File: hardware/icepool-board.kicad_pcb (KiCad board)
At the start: 4 copper layers, 66 x 65 mm, 181 parts, among them J1 8P8C_Shielded, J2 8P8C_Shielded, J3 I2C, J4 USB_B_Micro, J5 SWD, J6 PWR_IN, SW1 B3U-1000P, U1 ISL83488/ISL83490, U2 ATSAMD21E, U3 iCE40HX8K-BG121(121-Ball_caBG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, U4 iCE40HX8K-BG121(121-Ball_caBG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, U5 iCE40HX8K-BG121(121-Ball_caBG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, U6 iCE40HX8K-BG121(121-Ball_caBG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, U7 FAN2306, U8 TPS7150, U9 FAN2306, X1 CB3LV-3I-16M0000, X2 CB3LV-3I-16M0000, X3 CB3LV-3I-16M0000, X4 CB3LV-3I-16M0000, Y1 16MHz

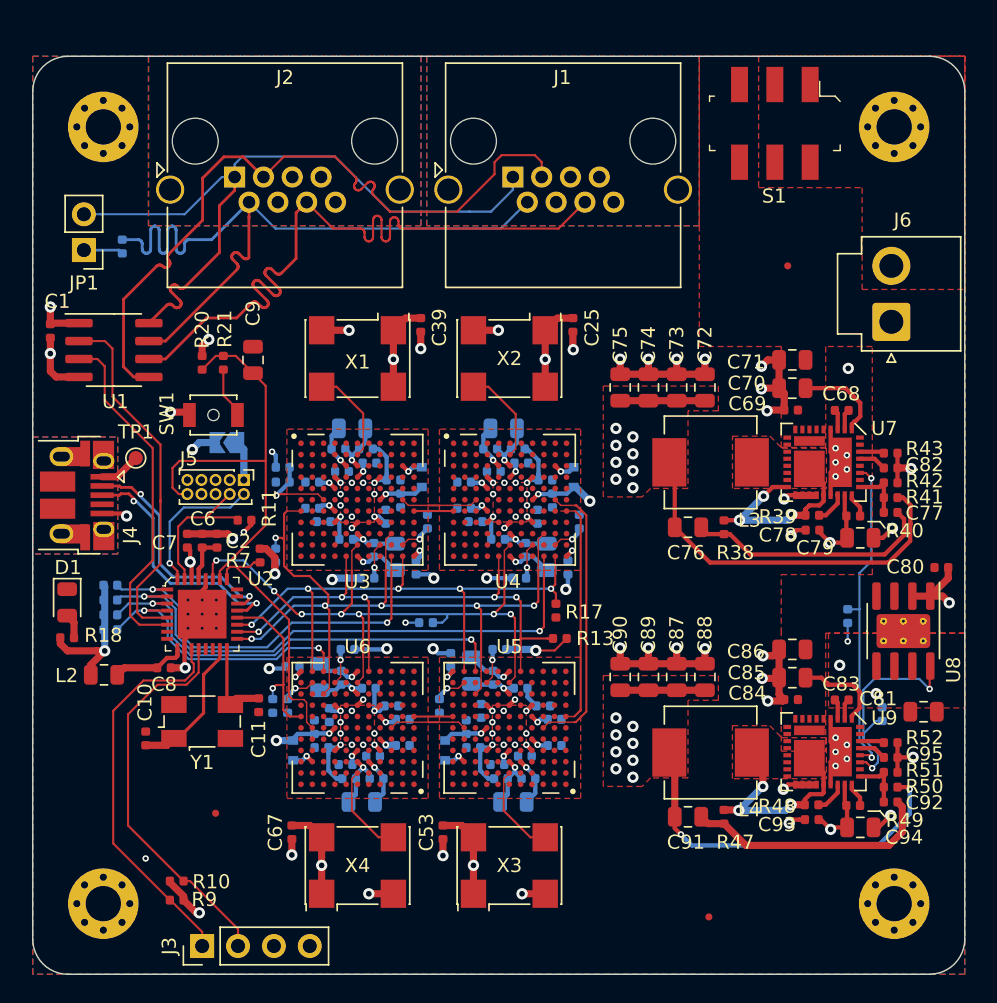
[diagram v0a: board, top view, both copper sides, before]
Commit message: Double checking buck layout, step 1.
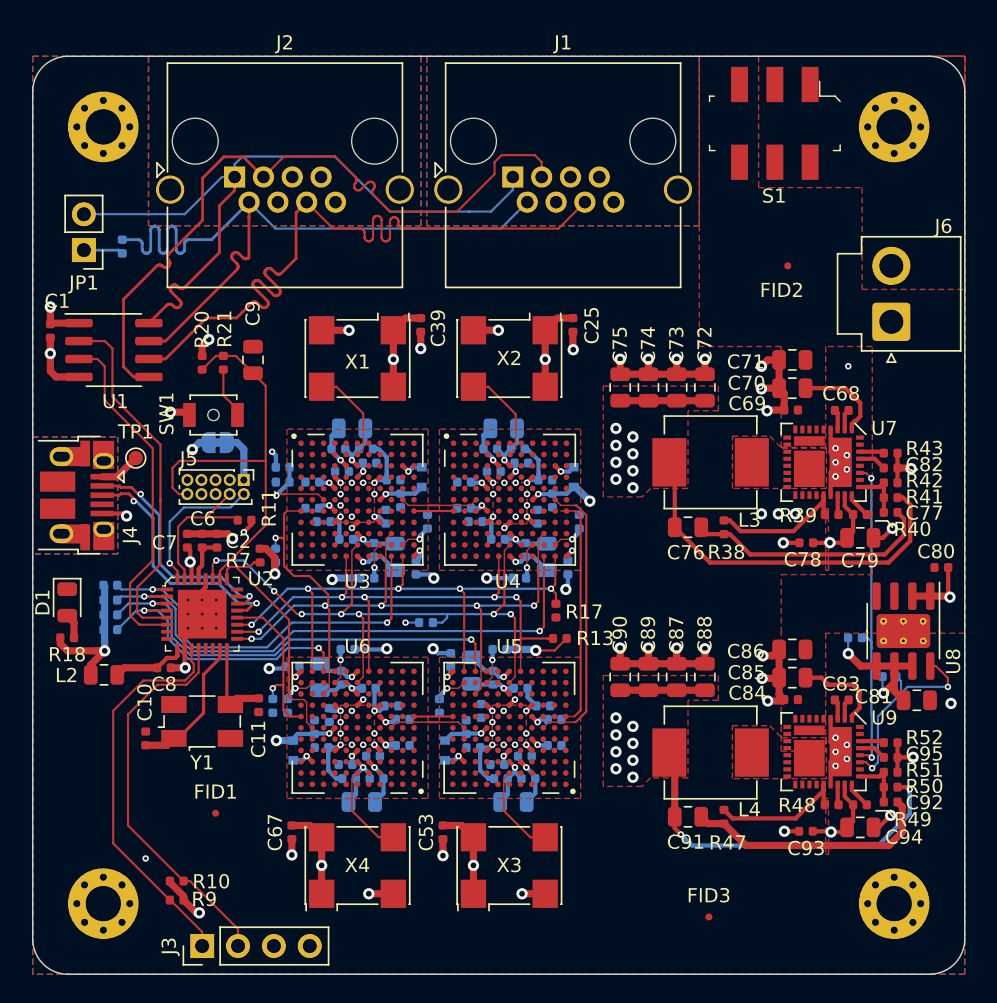
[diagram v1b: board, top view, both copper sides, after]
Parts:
- removed R12: 0R, Jumper:SolderJumper-2_P1.3mm_Open_TrianglePad1.0x1.5mm
- added JP2: SWD_VBUS, Jumper:SolderJumper-2_P1.3mm_Bridged_RoundedPad1.0x1.5mm, B.Cu at (123.1, 102.3)
- moved R44 2.70 mm to (170.7, 118.9), turned to 0 degrees
- moved R45 1.62 mm to (168.2, 116.2), turned to 0 degrees
- moved R48 1.42 mm to (166.6, 128.0)
- moved R39 1.38 mm to (166.6, 107.5)
- moved C78 1.00 mm to (164.8, 109.5)
- moved C81 0.94 mm to (172.6, 120.6)
- moved C93 0.92 mm to (164.8, 129.9)
- moved R40 0.49 mm to (168.6, 107.5)
- moved R49 0.48 mm to (168.6, 128.0)
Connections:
- net Net-(C68-Pad1) renamed /Power/SW_3v3
- net Net-(C83-Pad1) renamed /Power/SW_1v2
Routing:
- net +5V: track 45.9 -> 54.8 mm, vias 5 -> 4
- net /Power/SW_1v2: track 17.2 -> 11.5 mm, vias 3 -> 0
- net /Power/SW_3v3: track 16.5 -> 11.6 mm, vias 3 -> 0
- net GND: track 103.8 -> 101.2 mm, vias 77 -> 79
- net PG_0: track 16.2 -> 14.6 mm
- net Net-(R39-Pad2): track 2.31 -> 1.40 mm
- net Net-(R48-Pad2): track 2.30 -> 1.46 mm
- net Net-(J5-Pad1): track 2.85 -> 3.57 mm
- net +3V3: track 215.4 -> 214.9 mm
- added copper zone on B.Cu, net Net-(J1-PadSH)
- added copper zone on B.Cu, net Net-(J2-PadSH)
- removed copper zone on B.Cu, net (none)
- removed copper zone on F.Cu, net +5V

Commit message: Isolated F copper ground fill on power supplies.
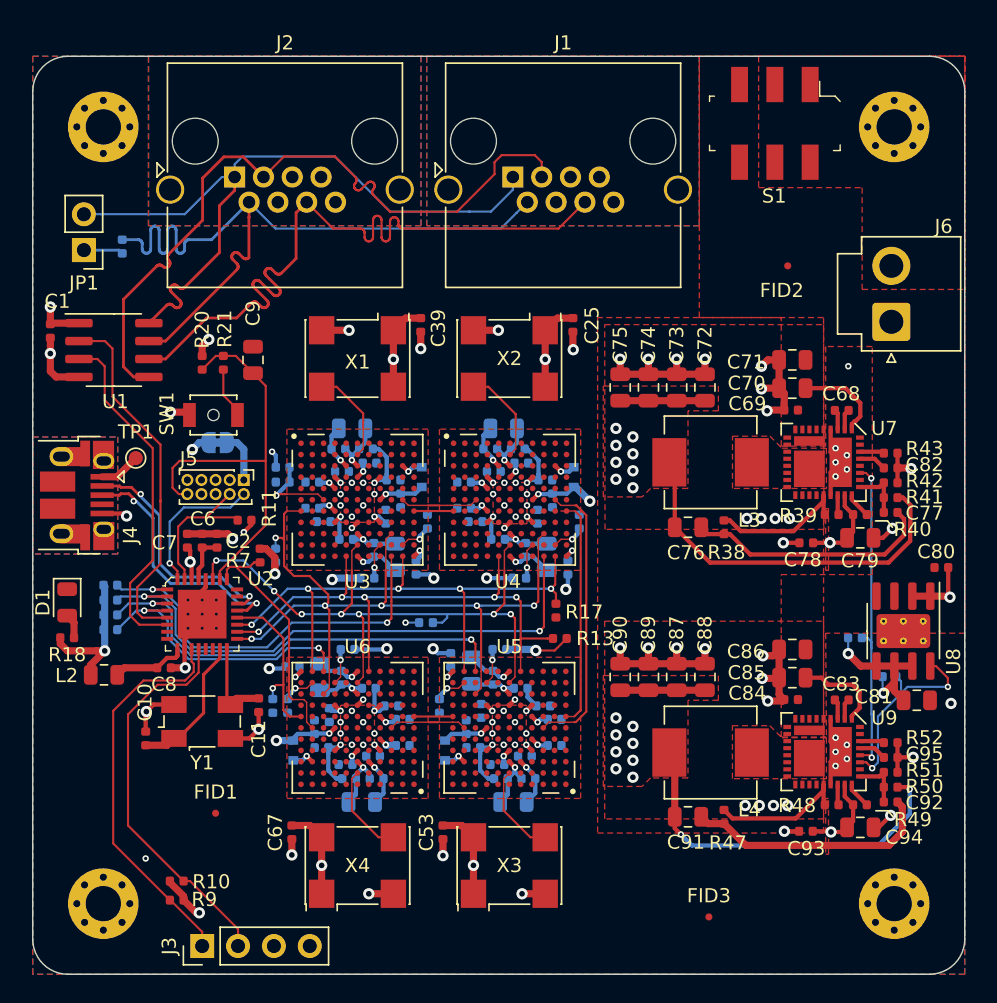
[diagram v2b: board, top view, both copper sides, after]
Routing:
- net GND: track 101.2 -> 108.3 mm, vias 79 -> 90
- net +3V3: track 214.9 -> 218.1 mm
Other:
- net class Default: clearance 0.127 -> 0.0889
- rule trace_clearance: 0.127 -> 0.0889

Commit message: Finalizing board.
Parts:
- added TP2: 3V3 Test, TestPoint:TestPoint_Pad_D1.0mm, F.Cu at (152.1, 108.0)
- added TP3: 5V Test, TestPoint:TestPoint_Pad_D1.0mm, F.Cu at (161.5, 112.8)
- added TP4: 1V2 Test, TestPoint:TestPoint_Pad_D1.0mm, F.Cu at (151.8, 128.7)
- moved FID3 6.89 mm to (151.8, 132.7)
- moved FID1 3.33 mm to (125.9, 127.0)
- moved R10 1.49 mm to (119.2, 132.3)
- moved R9 1.49 mm to (119.2, 133.7)
- moved C69 0.50 mm to (163.2, 100.0)
- moved C70 0.50 mm to (163.3, 98.5)
- moved C71 0.50 mm to (163.3, 96.5)
- moved C76 0.50 mm to (156.4, 108.8)
- moved C84 0.50 mm to (163.2, 120.5)
- moved C85 0.50 mm to (163.3, 119.0)
- moved C86 0.50 mm to (163.3, 117.0)
- moved C91 0.50 mm to (156.4, 129.3)
- moved R38 0.50 mm to (158.9, 108.8)
- moved R47 0.50 mm to (158.9, 129.3)
- moved J1 0.20 mm to (144.0, 83.3)
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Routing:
- net GND: track 108.3 -> 72.5 mm, vias 90 -> 67
- net +1V2: track 73.9 -> 79.8 mm
- net VCC: track 12.8 -> 6.96 mm
- net +5V: track 54.8 -> 60.3 mm, vias 4 -> 5
- net +3V3: track 218.1 -> 221.9 mm
- net /RX+: track 50.8 -> 53.5 mm
- net Net-(C91-Pad2): track 17.7 -> 19.2 mm, vias 0 -> 2
- net /Power/SW_1v2: track 11.5 -> 10.0 mm, vias 0 -> 2
- net /Power/SW_3v3: track 11.6 -> 10.5 mm, vias 0 -> 2
- net /TX+: track 51.0 -> 52.0 mm
- net /TX-: track 51.0 -> 52.0 mm
- net /RX-: track 54.7 -> 55.5 mm
- removed copper zone on B.Cu, net Net-(J1-PadSH)
- removed copper zone on F.Cu, net Net-(J1-PadSH)
- removed copper zone on In1.Cu, net Net-(J1-PadSH)
- removed copper zone on In2.Cu, net Net-(J1-PadSH)
- removed copper zone on B.Cu, net Net-(J2-PadSH)
- removed copper zone on F.Cu, net Net-(J2-PadSH)
- removed copper zone on In1.Cu, net Net-(J2-PadSH)
- removed copper zone on In2.Cu, net Net-(J2-PadSH)
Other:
- board text added: "+12V"
- board text added: "3V3"
- board text added: "GND"
- board text added: "SCL"
- board text added: "SDA"
- board text added: "icepool fourside.io"

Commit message: Generated gerbers. Ordered.
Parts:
- added FID4: Fiducial, Fiducial:Fiducial_0.5mm_Mask1mm, B.Cu at (166.8, 119.6)
- added FID5: Fiducial, Fiducial:Fiducial_0.5mm_Mask1mm, B.Cu at (138.6, 99.0)
- added FID6: Fiducial, Fiducial:Fiducial_0.5mm_Mask1mm, B.Cu at (135.3, 130.8)
- TP1, TP2, TP3, TP4: footprint TestPoint:TestPoint_Pad_D1.0mm -> TestPoint:TestPoint_Keystone_5000-5004_Miniature
- moved TP1 4.97 mm to (113.5, 100.2)
- moved TP2 2.40 mm to (152.2, 110.4)
- moved FID3 1.73 mm to (150.8, 134.2)
- moved TP4 1.56 mm to (151.6, 130.2)
- moved C69 0.30 mm to (163.2, 99.8)
- moved C70 0.30 mm to (163.3, 98.2)
- moved C71 0.30 mm to (163.3, 96.2)
- moved C84 0.30 mm to (163.2, 120.2)
- moved C85 0.30 mm to (163.3, 118.7)
- moved C86 0.30 mm to (163.3, 116.7)
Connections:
- J1 pad 4: (no net) -> Net-(J1-Pad4)
- J1 pad 5: (no net) -> Net-(J1-Pad5)
- J1 pad 7: (no net) -> Net-(J1-Pad7)
- J1 pad 8: (no net) -> Net-(J1-Pad8)
- J2 pad 4: (no net) -> Net-(J2-Pad4)
- J2 pad 5: (no net) -> Net-(J2-Pad5)
- J2 pad 7: (no net) -> Net-(J2-Pad7)
- J2 pad 8: (no net) -> Net-(J2-Pad8)
- J4 pad 4: (no net) -> Net-(J4-Pad4)
- J5 pad 6: (no net) -> Net-(J5-Pad6)
- J5 pad 8: (no net) -> Net-(J5-Pad8)
- S1 pad 1: (no net) -> Net-(S1-Pad1)
- S1 pad 4: (no net) -> Net-(S1-Pad4)
- U2 pad 13: (no net) -> Net-(U2-Pad13)
- U2 pad 14: (no net) -> Net-(U2-Pad14)
- U2 pad 23: (no net) -> Net-(U2-Pad23)
- U2 pad 24: (no net) -> Net-(U2-Pad24)
- U2 pad 7: (no net) -> Net-(U2-Pad7)
- U2 pad 8: (no net) -> Net-(U2-Pad8)
- U3 pad A1: (no net) -> Net-(U3-PadA1)
- U3 pad A10: (no net) -> Net-(U3-PadA10)
- U3 pad A11: (no net) -> Net-(U3-PadA11)
- U3 pad A2: (no net) -> Net-(U3-PadA2)
- U3 pad A3: (no net) -> Net-(U3-PadA3)
- U3 pad A4: (no net) -> Net-(U3-PadA4)
- U3 pad A5: (no net) -> Net-(U3-PadA5)
- U3 pad A6: (no net) -> Net-(U3-PadA6)
- U3 pad A7: (no net) -> Net-(U3-PadA7)
- U3 pad A8: (no net) -> Net-(U3-PadA8)
- U3 pad A9: (no net) -> Net-(U3-PadA9)
- U3 pad B1: (no net) -> Net-(U3-PadB1)
- U3 pad B10: (no net) -> Net-(U3-PadB10)
- U3 pad B11: (no net) -> Net-(U3-PadB11)
- U3 pad B2: (no net) -> Net-(U3-PadB2)
- U3 pad B3: (no net) -> Net-(U3-PadB3)
- U3 pad B4: (no net) -> Net-(U3-PadB4)
- U3 pad B5: (no net) -> Net-(U3-PadB5)
- U3 pad B7: (no net) -> Net-(U3-PadB7)
- U3 pad B8: (no net) -> Net-(U3-PadB8)
- U3 pad B9: (no net) -> Net-(U3-PadB9)
- U3 pad C1: (no net) -> Net-(U3-PadC1)
- U3 pad C11: (no net) -> Net-(U3-PadC11)
- U3 pad C2: (no net) -> Net-(U3-PadC2)
- U3 pad C3: (no net) -> Net-(U3-PadC3)
- U3 pad C4: (no net) -> Net-(U3-PadC4)
- U3 pad C7: (no net) -> Net-(U3-PadC7)
- U3 pad C8: (no net) -> Net-(U3-PadC8)
- U3 pad C9: (no net) -> Net-(U3-PadC9)
- U3 pad D1: (no net) -> Net-(U3-PadD1)
- U3 pad D10: (no net) -> Net-(U3-PadD10)
- U3 pad D11: (no net) -> Net-(U3-PadD11)
- U3 pad D2: (no net) -> Net-(U3-PadD2)
- U3 pad D3: (no net) -> Net-(U3-PadD3)
- U3 pad D5: (no net) -> Net-(U3-PadD5)
- U3 pad D7: (no net) -> Net-(U3-PadD7)
- U3 pad D9: (no net) -> Net-(U3-PadD9)
- U3 pad E1: (no net) -> Net-(U3-PadE1)
- U3 pad E10: (no net) -> Net-(U3-PadE10)
- U3 pad E11: (no net) -> Net-(U3-PadE11)
- U3 pad E2: (no net) -> Net-(U3-PadE2)
- U3 pad E3: (no net) -> Net-(U3-PadE3)
- U3 pad E8: (no net) -> Net-(U3-PadE8)
- U3 pad E9: (no net) -> Net-(U3-PadE9)
- U3 pad F1: (no net) -> Net-(U3-PadF1)
- U3 pad F11: (no net) -> Net-(U3-PadF11)
- U3 pad F2: (no net) -> Net-(U3-PadF2)
- U3 pad F4: (no net) -> Net-(U3-PadF4)
- U3 pad F9: (no net) -> Net-(U3-PadF9)
- U3 pad G10: (no net) -> Net-(U3-PadG10)
- U3 pad G2: (no net) -> Net-(U3-PadG2)
- U3 pad G3: (no net) -> Net-(U3-PadG3)
- U3 pad G8: (no net) -> Net-(U3-PadG8)
- U3 pad G9: (no net) -> Net-(U3-PadG9)
- U3 pad H1: (no net) -> Net-(U3-PadH1)
- U3 pad H10: (no net) -> Net-(U3-PadH10)
- U3 pad H11: (no net) -> Net-(U3-PadH11)
- U3 pad H2: (no net) -> Net-(U3-PadH2)
- U3 pad H3: (no net) -> Net-(U3-PadH3)
- U3 pad H7: (no net) -> Net-(U3-PadH7)
- U3 pad H9: (no net) -> Net-(U3-PadH9)
- U3 pad J1: (no net) -> Net-(U3-PadJ1)
- U3 pad J10: (no net) -> Net-(U3-PadJ10)
- U3 pad J11: (no net) -> Net-(U3-PadJ11)
- U3 pad J2: (no net) -> Net-(U3-PadJ2)
- U3 pad J3: (no net) -> Net-(U3-PadJ3)
- U3 pad J4: (no net) -> Net-(U3-PadJ4)
- U3 pad J5: (no net) -> Net-(U3-PadJ5)
- U3 pad J7: (no net) -> Net-(U3-PadJ7)
- U3 pad J8: (no net) -> Net-(U3-PadJ8)
- U3 pad K1: (no net) -> Net-(U3-PadK1)
- U3 pad K11: (no net) -> Net-(U3-PadK11)
- U3 pad K2: (no net) -> Net-(U3-PadK2)
- U3 pad K3: (no net) -> Net-(U3-PadK3)
- U3 pad K4: (no net) -> Net-(U3-PadK4)
- U3 pad K5: (no net) -> Net-(U3-PadK5)
- U3 pad K7: (no net) -> Net-(U3-PadK7)
- U3 pad K9: (no net) -> /ICE40HX8K-BG121_0/GMISO
- U3 pad L1: (no net) -> Net-(U3-PadL1)
- U3 pad L2: (no net) -> Net-(U3-PadL2)
- U3 pad L3: (no net) -> Net-(U3-PadL3)
- U3 pad L4: (no net) -> Net-(U3-PadL4)
- U3 pad L7: (no net) -> Net-(U3-PadL7)
- U3 pad L8: (no net) -> Net-(U3-PadL8)
- U4 pad A1: (no net) -> Net-(U4-PadA1)
- U4 pad A10: (no net) -> Net-(U4-PadA10)
- U4 pad A11: (no net) -> Net-(U4-PadA11)
- U4 pad A2: (no net) -> Net-(U4-PadA2)
- U4 pad A3: (no net) -> Net-(U4-PadA3)
- U4 pad A4: (no net) -> Net-(U4-PadA4)
- U4 pad A5: (no net) -> Net-(U4-PadA5)
- U4 pad A6: (no net) -> Net-(U4-PadA6)
- U4 pad A7: (no net) -> Net-(U4-PadA7)
- U4 pad A8: (no net) -> Net-(U4-PadA8)
- U4 pad A9: (no net) -> Net-(U4-PadA9)
- U4 pad B1: (no net) -> Net-(U4-PadB1)
- U4 pad B10: (no net) -> Net-(U4-PadB10)
- U4 pad B11: (no net) -> Net-(U4-PadB11)
- U4 pad B2: (no net) -> Net-(U4-PadB2)
- U4 pad B3: (no net) -> Net-(U4-PadB3)
- U4 pad B4: (no net) -> Net-(U4-PadB4)
- U4 pad B5: (no net) -> Net-(U4-PadB5)
- U4 pad B7: (no net) -> Net-(U4-PadB7)
- U4 pad B8: (no net) -> Net-(U4-PadB8)
- U4 pad B9: (no net) -> Net-(U4-PadB9)
- U4 pad C1: (no net) -> Net-(U4-PadC1)
- U4 pad C11: (no net) -> Net-(U4-PadC11)
- U4 pad C2: (no net) -> Net-(U4-PadC2)
- U4 pad C3: (no net) -> Net-(U4-PadC3)
- U4 pad C4: (no net) -> Net-(U4-PadC4)
- U4 pad C7: (no net) -> Net-(U4-PadC7)
- U4 pad C8: (no net) -> Net-(U4-PadC8)
- U4 pad C9: (no net) -> Net-(U4-PadC9)
- U4 pad D1: (no net) -> Net-(U4-PadD1)
- U4 pad D10: (no net) -> Net-(U4-PadD10)
- U4 pad D11: (no net) -> Net-(U4-PadD11)
- U4 pad D2: (no net) -> Net-(U4-PadD2)
- U4 pad D3: (no net) -> Net-(U4-PadD3)
- U4 pad D5: (no net) -> Net-(U4-PadD5)
- U4 pad D7: (no net) -> Net-(U4-PadD7)
- U4 pad D9: (no net) -> Net-(U4-PadD9)
- U4 pad E1: (no net) -> Net-(U4-PadE1)
- U4 pad E10: (no net) -> Net-(U4-PadE10)
- U4 pad E11: (no net) -> Net-(U4-PadE11)
- U4 pad E2: (no net) -> Net-(U4-PadE2)
- U4 pad E3: (no net) -> Net-(U4-PadE3)
- U4 pad E8: (no net) -> Net-(U4-PadE8)
- U4 pad E9: (no net) -> Net-(U4-PadE9)
- U4 pad F1: (no net) -> Net-(U4-PadF1)
- U4 pad F11: (no net) -> Net-(U4-PadF11)
- U4 pad F2: (no net) -> Net-(U4-PadF2)
- U4 pad F4: (no net) -> Net-(U4-PadF4)
- U4 pad F9: (no net) -> Net-(U4-PadF9)
- U4 pad G10: (no net) -> Net-(U4-PadG10)
- U4 pad G2: (no net) -> Net-(U4-PadG2)
- U4 pad G3: (no net) -> Net-(U4-PadG3)
- U4 pad G8: (no net) -> Net-(U4-PadG8)
- U4 pad G9: (no net) -> Net-(U4-PadG9)
- U4 pad H1: (no net) -> Net-(U4-PadH1)
- U4 pad H10: (no net) -> Net-(U4-PadH10)
- U4 pad H11: (no net) -> Net-(U4-PadH11)
- U4 pad H2: (no net) -> Net-(U4-PadH2)
- U4 pad H3: (no net) -> Net-(U4-PadH3)
- U4 pad H7: (no net) -> Net-(U4-PadH7)
- U4 pad H9: (no net) -> Net-(U4-PadH9)
- U4 pad J1: (no net) -> Net-(U4-PadJ1)
- U4 pad J10: (no net) -> Net-(U4-PadJ10)
- U4 pad J11: (no net) -> Net-(U4-PadJ11)
- U4 pad J2: (no net) -> Net-(U4-PadJ2)
- U4 pad J3: (no net) -> Net-(U4-PadJ3)
- U4 pad J4: (no net) -> Net-(U4-PadJ4)
- U4 pad J5: (no net) -> Net-(U4-PadJ5)
- U4 pad J7: (no net) -> Net-(U4-PadJ7)
- U4 pad J8: (no net) -> Net-(U4-PadJ8)
- U4 pad K1: (no net) -> Net-(U4-PadK1)
- U4 pad K11: (no net) -> Net-(U4-PadK11)
- U4 pad K2: (no net) -> Net-(U4-PadK2)
- U4 pad K3: (no net) -> Net-(U4-PadK3)
- U4 pad K4: (no net) -> Net-(U4-PadK4)
- U4 pad K5: (no net) -> Net-(U4-PadK5)
- U4 pad K7: (no net) -> Net-(U4-PadK7)
- U4 pad K9: (no net) -> /ICE40HX8K-BG121_1/GMISO
- U4 pad L1: (no net) -> Net-(U4-PadL1)
- U4 pad L2: (no net) -> Net-(U4-PadL2)
- U4 pad L3: (no net) -> Net-(U4-PadL3)
- U4 pad L4: (no net) -> Net-(U4-PadL4)
- U4 pad L7: (no net) -> Net-(U4-PadL7)
- U4 pad L8: (no net) -> Net-(U4-PadL8)
- U5 pad A1: (no net) -> Net-(U5-PadA1)
- U5 pad A10: (no net) -> Net-(U5-PadA10)
- U5 pad A11: (no net) -> Net-(U5-PadA11)
- U5 pad A2: (no net) -> Net-(U5-PadA2)
- U5 pad A3: (no net) -> Net-(U5-PadA3)
- U5 pad A4: (no net) -> Net-(U5-PadA4)
- U5 pad A5: (no net) -> Net-(U5-PadA5)
- U5 pad A6: (no net) -> Net-(U5-PadA6)
- U5 pad A7: (no net) -> Net-(U5-PadA7)
- U5 pad A8: (no net) -> Net-(U5-PadA8)
- U5 pad A9: (no net) -> Net-(U5-PadA9)
- U5 pad B1: (no net) -> Net-(U5-PadB1)
- U5 pad B10: (no net) -> Net-(U5-PadB10)
- U5 pad B11: (no net) -> Net-(U5-PadB11)
- U5 pad B2: (no net) -> Net-(U5-PadB2)
- U5 pad B3: (no net) -> Net-(U5-PadB3)
- U5 pad B4: (no net) -> Net-(U5-PadB4)
- U5 pad B5: (no net) -> Net-(U5-PadB5)
- U5 pad B7: (no net) -> Net-(U5-PadB7)
- U5 pad B8: (no net) -> Net-(U5-PadB8)
- U5 pad B9: (no net) -> Net-(U5-PadB9)
- U5 pad C1: (no net) -> Net-(U5-PadC1)
- U5 pad C11: (no net) -> Net-(U5-PadC11)
- U5 pad C2: (no net) -> Net-(U5-PadC2)
- U5 pad C3: (no net) -> Net-(U5-PadC3)
- U5 pad C4: (no net) -> Net-(U5-PadC4)
- U5 pad C7: (no net) -> Net-(U5-PadC7)
- U5 pad C8: (no net) -> Net-(U5-PadC8)
- U5 pad C9: (no net) -> Net-(U5-PadC9)
- U5 pad D1: (no net) -> Net-(U5-PadD1)
- U5 pad D10: (no net) -> Net-(U5-PadD10)
- U5 pad D11: (no net) -> Net-(U5-PadD11)
- U5 pad D2: (no net) -> Net-(U5-PadD2)
- U5 pad D3: (no net) -> Net-(U5-PadD3)
- U5 pad D5: (no net) -> Net-(U5-PadD5)
- U5 pad D7: (no net) -> Net-(U5-PadD7)
- U5 pad D9: (no net) -> Net-(U5-PadD9)
- U5 pad E1: (no net) -> Net-(U5-PadE1)
- U5 pad E10: (no net) -> Net-(U5-PadE10)
- U5 pad E11: (no net) -> Net-(U5-PadE11)
- U5 pad E2: (no net) -> Net-(U5-PadE2)
- U5 pad E3: (no net) -> Net-(U5-PadE3)
- U5 pad E8: (no net) -> Net-(U5-PadE8)
- U5 pad E9: (no net) -> Net-(U5-PadE9)
- U5 pad F1: (no net) -> Net-(U5-PadF1)
- U5 pad F11: (no net) -> Net-(U5-PadF11)
- U5 pad F2: (no net) -> Net-(U5-PadF2)
- U5 pad F4: (no net) -> Net-(U5-PadF4)
- U5 pad F9: (no net) -> Net-(U5-PadF9)
- U5 pad G10: (no net) -> Net-(U5-PadG10)
- U5 pad G2: (no net) -> Net-(U5-PadG2)
- U5 pad G3: (no net) -> Net-(U5-PadG3)
- U5 pad G8: (no net) -> Net-(U5-PadG8)
- U5 pad G9: (no net) -> Net-(U5-PadG9)
- U5 pad H1: (no net) -> Net-(U5-PadH1)
- U5 pad H10: (no net) -> Net-(U5-PadH10)
- U5 pad H11: (no net) -> Net-(U5-PadH11)
- U5 pad H2: (no net) -> Net-(U5-PadH2)
- U5 pad H3: (no net) -> Net-(U5-PadH3)
- U5 pad H7: (no net) -> Net-(U5-PadH7)
- U5 pad H9: (no net) -> Net-(U5-PadH9)
- U5 pad J1: (no net) -> Net-(U5-PadJ1)
- U5 pad J10: (no net) -> Net-(U5-PadJ10)
- U5 pad J11: (no net) -> Net-(U5-PadJ11)
- U5 pad J2: (no net) -> Net-(U5-PadJ2)
- U5 pad J3: (no net) -> Net-(U5-PadJ3)
- U5 pad J4: (no net) -> Net-(U5-PadJ4)
- U5 pad J5: (no net) -> Net-(U5-PadJ5)
- U5 pad J7: (no net) -> Net-(U5-PadJ7)
- U5 pad J8: (no net) -> Net-(U5-PadJ8)
- U5 pad K1: (no net) -> Net-(U5-PadK1)
- U5 pad K11: (no net) -> Net-(U5-PadK11)
- U5 pad K2: (no net) -> Net-(U5-PadK2)
- U5 pad K3: (no net) -> Net-(U5-PadK3)
- U5 pad K4: (no net) -> Net-(U5-PadK4)
- U5 pad K5: (no net) -> Net-(U5-PadK5)
- U5 pad K7: (no net) -> Net-(U5-PadK7)
- U5 pad K9: (no net) -> /ICE40HX8K-BG121_2/GMISO
- U5 pad L1: (no net) -> Net-(U5-PadL1)
- U5 pad L2: (no net) -> Net-(U5-PadL2)
- U5 pad L3: (no net) -> Net-(U5-PadL3)
- U5 pad L4: (no net) -> Net-(U5-PadL4)
- U5 pad L7: (no net) -> Net-(U5-PadL7)
- U5 pad L8: (no net) -> Net-(U5-PadL8)
- U6 pad A1: (no net) -> Net-(U6-PadA1)
- U6 pad A10: (no net) -> Net-(U6-PadA10)
- U6 pad A11: (no net) -> Net-(U6-PadA11)
- U6 pad A2: (no net) -> Net-(U6-PadA2)
- U6 pad A3: (no net) -> Net-(U6-PadA3)
- U6 pad A4: (no net) -> Net-(U6-PadA4)
- U6 pad A5: (no net) -> Net-(U6-PadA5)
- U6 pad A6: (no net) -> Net-(U6-PadA6)
- U6 pad A7: (no net) -> Net-(U6-PadA7)
- U6 pad A8: (no net) -> Net-(U6-PadA8)
- U6 pad A9: (no net) -> Net-(U6-PadA9)
- U6 pad B1: (no net) -> Net-(U6-PadB1)
- U6 pad B10: (no net) -> Net-(U6-PadB10)
- U6 pad B11: (no net) -> Net-(U6-PadB11)
- U6 pad B2: (no net) -> Net-(U6-PadB2)
- U6 pad B3: (no net) -> Net-(U6-PadB3)
- U6 pad B4: (no net) -> Net-(U6-PadB4)
- U6 pad B5: (no net) -> Net-(U6-PadB5)
- U6 pad B7: (no net) -> Net-(U6-PadB7)
- U6 pad B8: (no net) -> Net-(U6-PadB8)
- U6 pad B9: (no net) -> Net-(U6-PadB9)
- U6 pad C1: (no net) -> Net-(U6-PadC1)
- U6 pad C11: (no net) -> Net-(U6-PadC11)
- U6 pad C2: (no net) -> Net-(U6-PadC2)
- U6 pad C3: (no net) -> Net-(U6-PadC3)
- U6 pad C4: (no net) -> Net-(U6-PadC4)
- U6 pad C7: (no net) -> Net-(U6-PadC7)
- U6 pad C8: (no net) -> Net-(U6-PadC8)
- U6 pad C9: (no net) -> Net-(U6-PadC9)
- U6 pad D1: (no net) -> Net-(U6-PadD1)
- U6 pad D10: (no net) -> Net-(U6-PadD10)
- U6 pad D11: (no net) -> Net-(U6-PadD11)
- U6 pad D2: (no net) -> Net-(U6-PadD2)
- U6 pad D3: (no net) -> Net-(U6-PadD3)
- U6 pad D5: (no net) -> Net-(U6-PadD5)
- U6 pad D7: (no net) -> Net-(U6-PadD7)
- U6 pad D9: (no net) -> Net-(U6-PadD9)
- U6 pad E1: (no net) -> Net-(U6-PadE1)
- U6 pad E10: (no net) -> Net-(U6-PadE10)
- U6 pad E11: (no net) -> Net-(U6-PadE11)
- U6 pad E2: (no net) -> Net-(U6-PadE2)
- U6 pad E3: (no net) -> Net-(U6-PadE3)
- U6 pad E8: (no net) -> Net-(U6-PadE8)
- U6 pad E9: (no net) -> Net-(U6-PadE9)
- U6 pad F1: (no net) -> Net-(U6-PadF1)
- U6 pad F11: (no net) -> Net-(U6-PadF11)
- U6 pad F2: (no net) -> Net-(U6-PadF2)
- U6 pad F4: (no net) -> Net-(U6-PadF4)
- U6 pad F9: (no net) -> Net-(U6-PadF9)
- U6 pad G10: (no net) -> Net-(U6-PadG10)
- U6 pad G2: (no net) -> Net-(U6-PadG2)
- U6 pad G3: (no net) -> Net-(U6-PadG3)
- U6 pad G8: (no net) -> Net-(U6-PadG8)
- U6 pad G9: (no net) -> Net-(U6-PadG9)
- U6 pad H1: (no net) -> Net-(U6-PadH1)
- U6 pad H10: (no net) -> Net-(U6-PadH10)
- U6 pad H11: (no net) -> Net-(U6-PadH11)
- U6 pad H2: (no net) -> Net-(U6-PadH2)
- U6 pad H3: (no net) -> Net-(U6-PadH3)
- U6 pad H7: (no net) -> Net-(U6-PadH7)
- U6 pad H9: (no net) -> Net-(U6-PadH9)
- U6 pad J1: (no net) -> Net-(U6-PadJ1)
- U6 pad J10: (no net) -> Net-(U6-PadJ10)
- U6 pad J11: (no net) -> Net-(U6-PadJ11)
- U6 pad J2: (no net) -> Net-(U6-PadJ2)
- U6 pad J3: (no net) -> Net-(U6-PadJ3)
- U6 pad J4: (no net) -> Net-(U6-PadJ4)
- U6 pad J5: (no net) -> Net-(U6-PadJ5)
- U6 pad J7: (no net) -> Net-(U6-PadJ7)
- U6 pad J8: (no net) -> Net-(U6-PadJ8)
- U6 pad K1: (no net) -> Net-(U6-PadK1)
- U6 pad K11: (no net) -> Net-(U6-PadK11)
- U6 pad K2: (no net) -> Net-(U6-PadK2)
- U6 pad K3: (no net) -> Net-(U6-PadK3)
- U6 pad K4: (no net) -> Net-(U6-PadK4)
- U6 pad K5: (no net) -> Net-(U6-PadK5)
- U6 pad K7: (no net) -> Net-(U6-PadK7)
- U6 pad K9: (no net) -> /ICE40HX8K-BG121_3/GMISO
- U6 pad L1: (no net) -> Net-(U6-PadL1)
- U6 pad L2: (no net) -> Net-(U6-PadL2)
- U6 pad L3: (no net) -> Net-(U6-PadL3)
- U6 pad L4: (no net) -> Net-(U6-PadL4)
- U6 pad L7: (no net) -> Net-(U6-PadL7)
- U6 pad L8: (no net) -> Net-(U6-PadL8)
- U7 pad 28: (no net) -> Net-(U7-Pad28)
- U7 pad 30: (no net) -> PG_2
- U7 pad 33: (no net) -> Net-(U7-Pad33)
- U7 pad 34: (no net) -> Net-(U7-Pad34)
- U9 pad 28: (no net) -> Net-(U9-Pad28)
- U9 pad 33: (no net) -> Net-(U9-Pad33)
- U9 pad 34: (no net) -> Net-(U9-Pad34)
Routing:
- net VCC: track 6.96 -> 0.00 mm
- net Net-(J4-Pad1): track 2.93 -> 8.16 mm
- net +3V3: track 221.9 -> 224.3 mm, vias 51 -> 59
- net GND: track 72.5 -> 74.4 mm, vias 67 -> 119
- net +1V2: track 79.8 -> 80.9 mm, vias 26 -> 34
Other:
- rule via_min_size: 0.2 -> 0.23
- board text added: "+1V2"
- board text added: "+3V3"
- board text added: "+5V"
- board text added: "VBUS"
- board text added: "icepool-board 201911-0 fourside.io"
- board text removed: "icepool fourside.io"

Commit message: SWD header is 1.27mm pitch, not 1.00mm (Oops.)
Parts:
- J5: footprint Connector_PinHeader_1.00mm:PinHeader_2x05_P1.00mm_Vertical -> Connector_PinHeader_1.27mm:PinHeader_2x05_P1.27mm_Vertical
- moved J5 0.92 mm to (125.7, 104.4)
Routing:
- net /SWD_CLK: track 10.8 -> 11.7 mm
- net /SWD_IO: track 10.4 -> 11.2 mm

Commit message: Moved i2c.
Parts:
- R10, R9: moved to B.Cu
- moved J3 18.5 mm to (112.5, 122.1), turned to 0 degrees
- moved R9 12.4 mm to (115.0, 122.0)
- moved R10 10.0 mm to (115.0, 123.2), turned to 180 degrees
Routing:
- net /I2C_SDA: track 28.0 -> 14.1 mm
- net /I2C_SCL: track 27.8 -> 16.0 mm
- net +3V3: track 224.8 -> 223.7 mm
- net GND: vias 119 -> 118

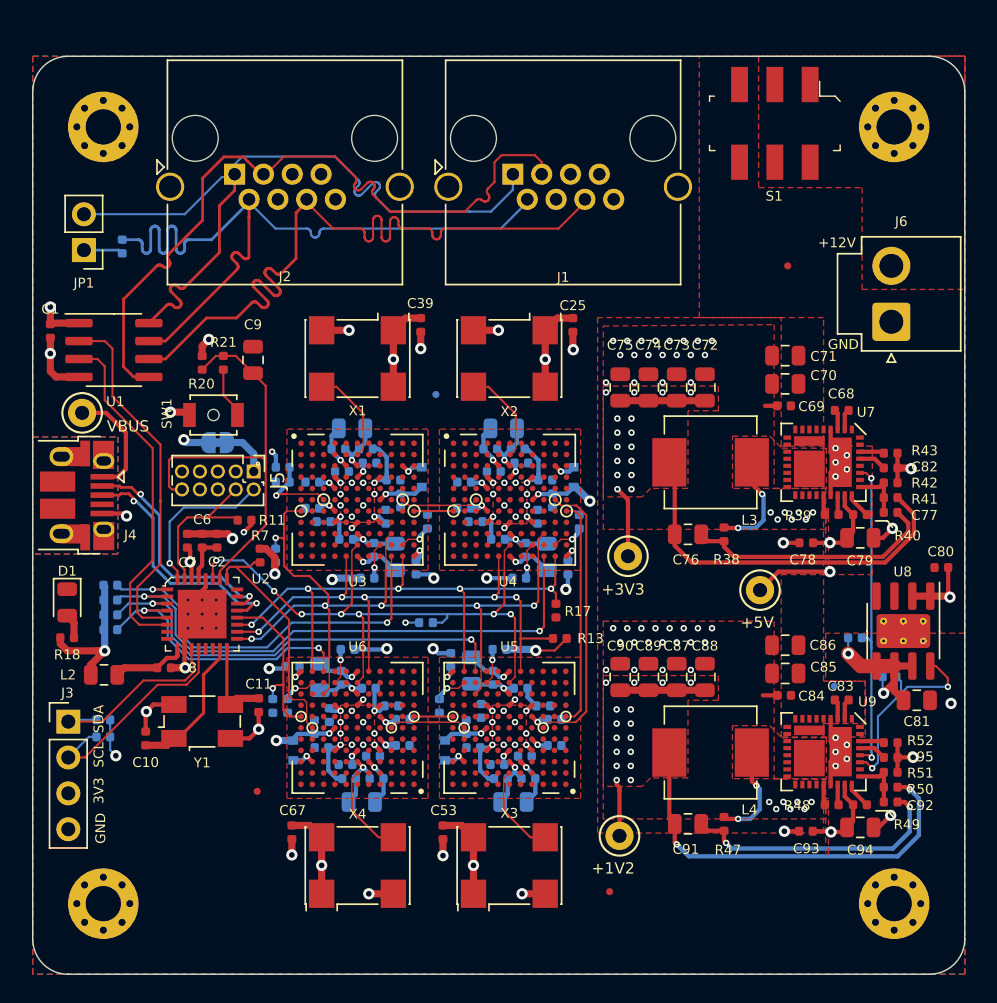
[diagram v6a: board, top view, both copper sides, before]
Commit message: Updated some passive sizes. Replaced term jumper with handsolder.
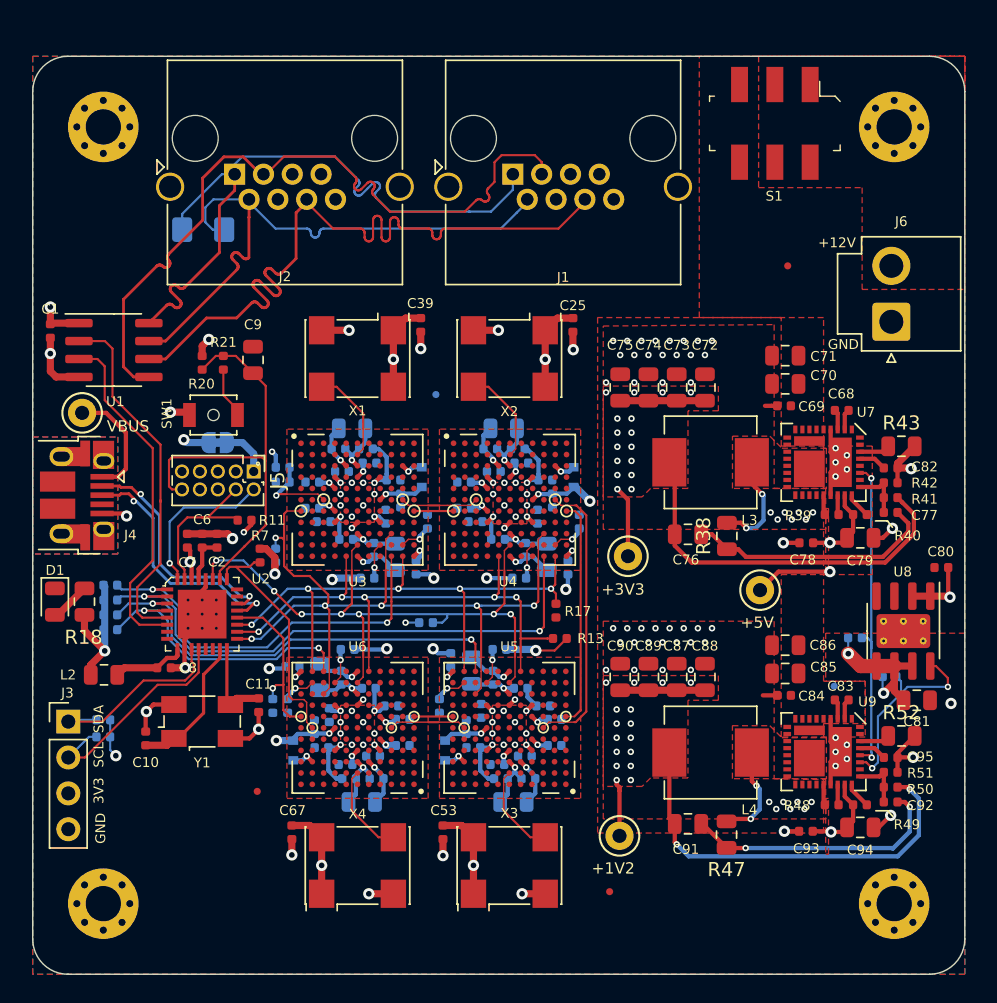
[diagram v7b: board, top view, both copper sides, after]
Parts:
- removed JP1: RS485-Term, Connector_PinHeader_2.54mm:PinHeader_1x02_P2.54mm_Vertical
- R18, R38, R43, R47, R52: footprint Resistor_SMD:R_0402_1005Metric -> Resistor_SMD:R_0805_2012Metric
- R21: value 1k -> 4k7
- R6: footprint Resistor_SMD:R_0402_1005Metric -> Resistor_SMD:R_1206_3216Metric_Pad1.42x1.75mm_HandSolder
- moved R6 5.86 mm to (122.1, 87.3), turned to 0 degrees
- moved R18 2.83 mm to (113.7, 113.6), turned to 90 degrees
- moved R43 0.90 mm to (171.5, 102.6)
- moved R52 0.90 mm to (171.5, 123.1)
- moved D1 0.87 mm to (111.6, 113.6)
- moved R47 0.78 mm to (159.1, 130.1)
- moved R38 0.24 mm to (159.2, 109.0)
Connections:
- R6 pad 1: Net-(JP1-Pad1) -> /RX+
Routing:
- net /RX-: track 55.5 -> 43.2 mm
- net /RX+: track 53.5 -> 47.7 mm
- net Net-(JP1-Pad1): track 2.81 -> 0.00 mm
- net GND: track 74.4 -> 76.4 mm
- net Net-(D1-Pad2): track 1.76 -> 2.87 mm
- net +3V3: track 223.7 -> 223.0 mm
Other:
- board text added: "icepool-board 202001-0 fourside.io"
- board text removed: "icepool-board 201911-0 fourside.io"
